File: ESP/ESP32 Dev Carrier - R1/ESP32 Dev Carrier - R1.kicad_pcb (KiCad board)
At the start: 4 copper layers, 75 x 75 mm, 57 parts, among them J1 Conn_01x02, J2 USB_B_Micro, J3 Conn_02x20_Top_Bottom, J4 Conn_01x05, J5 Conn_01x05, J6 Conn_01x05, Q1 MMS9013, Q2 MMS9013, SW1 SW_Push, U1 ESP32-WROVER-B_(16MB)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

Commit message: Blurgh. Almost ready to order.
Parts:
- added D10: BAT54S, Package_TO_SOT_SMD:SOT-23, F.Cu at (39.7, 44.1)
- added D11: BAT54S, Package_TO_SOT_SMD:SOT-23, F.Cu at (39.7, 34.0)
- added D13: BAT54S, Package_TO_SOT_SMD:SOT-23, F.Cu at (43.9, 36.5)
- added D14: BAT54S, Package_TO_SOT_SMD:SOT-23, F.Cu at (43.9, 41.6)
- added D15: BAT54S, Package_TO_SOT_SMD:SOT-23, F.Cu at (39.7, 39.0)
- added D16: BAT54S, Package_TO_SOT_SMD:SOT-23, F.Cu at (44.2, 11.8)
- added D17: BAT54S, Package_TO_SOT_SMD:SOT-23, F.Cu at (44.2, 15.6)
- added D5: BAT54S, Package_TO_SOT_SMD:SOT-23, F.Cu at (43.9, 51.7)
- added D6: BAT54S, Package_TO_SOT_SMD:SOT-23, F.Cu at (39.7, 49.2)
- added D9: BAT54S, Package_TO_SOT_SMD:SOT-23, F.Cu at (43.9, 46.7)
- added J10: Conn_01x09, Connector_JST:JST_XH_B9B-XH-A_1x09_P2.50mm_Vertical, F.Cu at (71.2, 34.2)
- added J11: Conn_01x04, Connector_JST:JST_XH_B4B-XH-A_1x04_P2.50mm_Vertical, F.Cu at (50.1, 20.1)
- added J12: Conn_01x04, Connector_JST:JST_XH_B4B-XH-A_1x04_P2.50mm_Vertical, F.Cu at (57.1, 20.0)
- added J13: Conn_01x04, Connector_JST:JST_XH_B4B-XH-A_1x04_P2.50mm_Vertical, F.Cu at (71.1, 20.1)
- added J14: Conn_01x04, Connector_JST:JST_XH_B4B-XH-A_1x04_P2.50mm_Vertical, F.Cu at (64.1, 20.1)
- added J7: Conn_01x09, Connector_JST:JST_XH_B9B-XH-A_1x09_P2.50mm_Vertical, F.Cu at (50.2, 34.2)
- added J8: Conn_01x09, Connector_JST:JST_XH_B9B-XH-A_1x09_P2.50mm_Vertical, F.Cu at (57.2, 34.2)
- added J9: Conn_01x09, Connector_JST:JST_XH_B9B-XH-A_1x09_P2.50mm_Vertical, F.Cu at (64.2, 34.2)
- added R18: 4.7K, Resistor_SMD:R_0603_1608Metric, F.Cu at (68.6, 60.0)
- added R19: 4.7K, Resistor_SMD:R_0603_1608Metric, F.Cu at (66.7, 60.0)
- added R20: 4.7K, Resistor_SMD:R_0603_1608Metric, F.Cu at (60.4, 60.0)
- added R21: 4.7K, Resistor_SMD:R_0603_1608Metric, F.Cu at (62.3, 60.0)
- added R22: 4.7K, Resistor_SMD:R_0603_1608Metric, F.Cu at (69.9, 14.9)
- added R23: 4.7K, Resistor_SMD:R_0603_1608Metric, F.Cu at (44.5, 29.5)
- D1: footprint Diode_SMD:D_SMA -> Diode_SMD:D_SMC
- J4, J5, J6: footprint Connector_JST:JST_XH_B5B-XH-AM_1x05_P2.50mm_Vertical -> Connector_JST:JST_XH_B5B-XH-A_1x05_P2.50mm_Vertical
- moved D8 62.7 mm to (63.5, 70.0)
- moved D12 62.4 mm to (61.6, 70.0)
- moved R27 62.4 mm to (63.5, 66.3)
- moved R10 62.1 mm to (61.6, 66.3)
- moved D3 47.8 mm to (57.8, 70.2)
- moved D4 47.4 mm to (55.9, 70.2)
- moved R13 42.7 mm to (57.8, 66.3)
- moved R16 42.3 mm to (55.9, 66.3)
- moved D7 36.7 mm to (59.7, 70.0)
- moved R26 36.7 mm to (59.7, 66.3)
- moved R14 25.7 mm to (69.9, 8.56), turned to 0 degrees
- moved R15 25.2 mm to (69.9, 11.1), turned to 0 degrees
- moved R6 25.1 mm to (43.9, 22.2), turned to -90 degrees
- moved R5 14.8 mm to (42.2, 22.2)
- moved J4 10.1 mm to (64.7, 3.64), turned to -90 degrees
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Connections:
- net Net-(J3-Pad27) renamed /IO4
- net Net-(J3-Pad29) renamed /IO2
- D3 pad 2: Net-(D3-Pad2) -> +3V3
- D4 pad 2: Net-(D4-Pad2) -> +3V3
- J3 pad 11: Net-(J3-Pad11) -> Net-(D10-Pad3)
- J4 pad 3: Net-(D2-Pad2) -> Net-(D2-Pad1)
- J4 pad 4: Net-(D2-Pad1) -> Net-(D2-Pad2)
- J5 pad 3: Net-(D2-Pad2) -> Net-(D2-Pad1)
- J5 pad 4: Net-(D2-Pad1) -> Net-(D2-Pad2)
- J6 pad 3: Net-(D2-Pad2) -> Net-(D2-Pad1)
- J6 pad 4: Net-(D2-Pad1) -> Net-(D2-Pad2)
- R13 pad 1: Net-(D3-Pad2) -> Net-(R13-Pad1)
- R13 pad 2: +3V3 -> Net-(D3-Pad1)
- R16 pad 1: Net-(D4-Pad2) -> Net-(R16-Pad1)
- R16 pad 2: +3V3 -> Net-(D4-Pad1)
- R27 pad 2: Net-(J3-Pad11) -> Net-(J3-Pad15)
- U1 pad 8: Net-(J3-Pad11) -> Net-(D10-Pad3)
- U4 pad 18: Net-(D4-Pad1) -> Net-(R16-Pad1)
- U4 pad 19: Net-(D3-Pad1) -> Net-(R13-Pad1)
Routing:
- net +5V: track 72.8 -> 223.0 mm, vias 5 -> 4
- net Net-(D10-Pad3): track 0.00 -> 100.6 mm, vias 0 -> 1
- net Net-(D11-Pad3): track 49.1 -> 140.5 mm, vias 1 -> 2
- net Net-(D13-Pad3): track 44.9 -> 128.5 mm, vias 1 -> 2
- net Net-(D15-Pad3): track 27.4 -> 107.8 mm, vias 1 -> 2
- net Net-(D14-Pad3): track 24.3 -> 101.7 mm, vias 1 -> 2
- net Net-(D5-Pad3): track 24.3 -> 100.5 mm
- net Net-(D6-Pad3): track 27.4 -> 103.2 mm
- net Net-(J3-Pad15): track 27.6 -> 101.9 mm
- net Net-(D9-Pad3): track 24.3 -> 98.4 mm
- net Net-(J3-Pad18): track 30.2 -> 91.9 mm
- net Net-(R13-Pad1): track 0.00 -> 56.8 mm
- net Net-(R16-Pad1): track 0.00 -> 55.1 mm
- net Net-(D17-Pad3): track 52.3 -> 105.4 mm
- net Net-(D16-Pad3): track 49.3 -> 98.1 mm
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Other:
- outline, holes or cut-outs redrawn
- board text added: "ESP32 DevCarrier"
- board text removed: "ESP32 DevBoard"

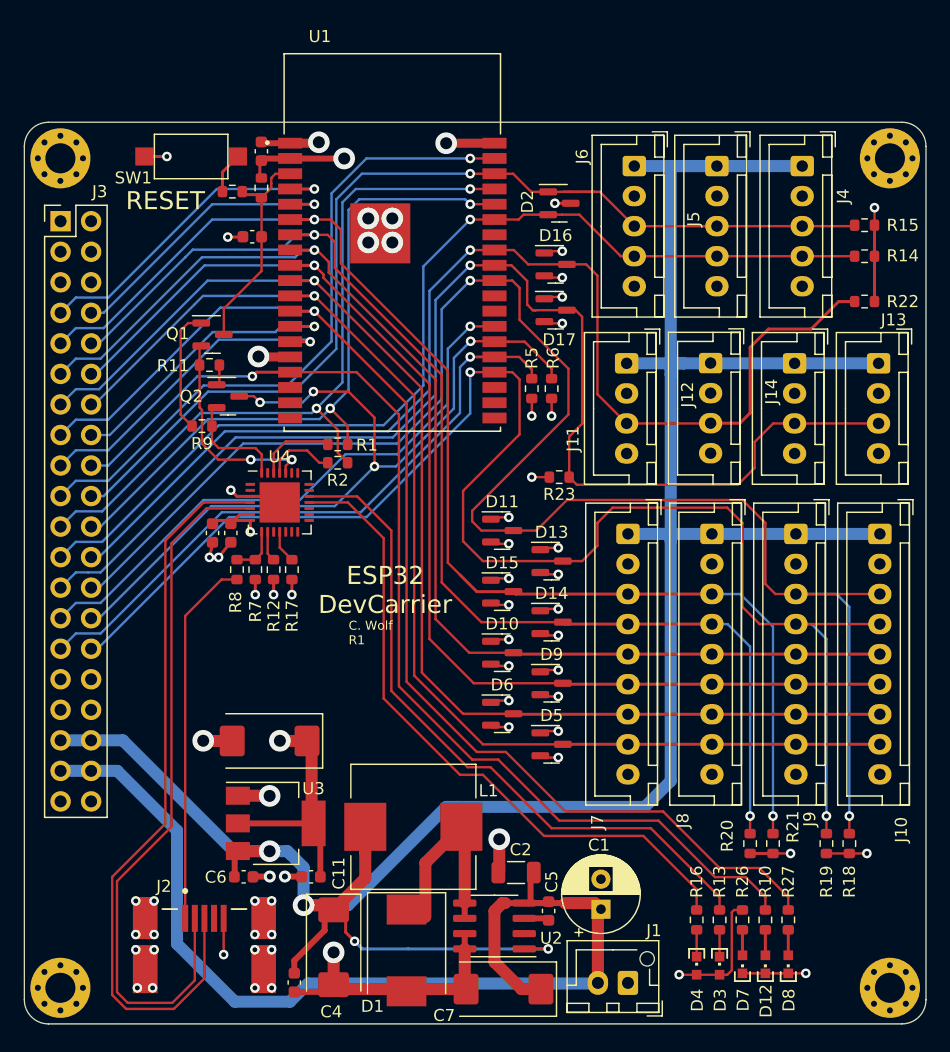
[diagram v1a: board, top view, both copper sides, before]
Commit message: Reworking things to use the new controller PCB.
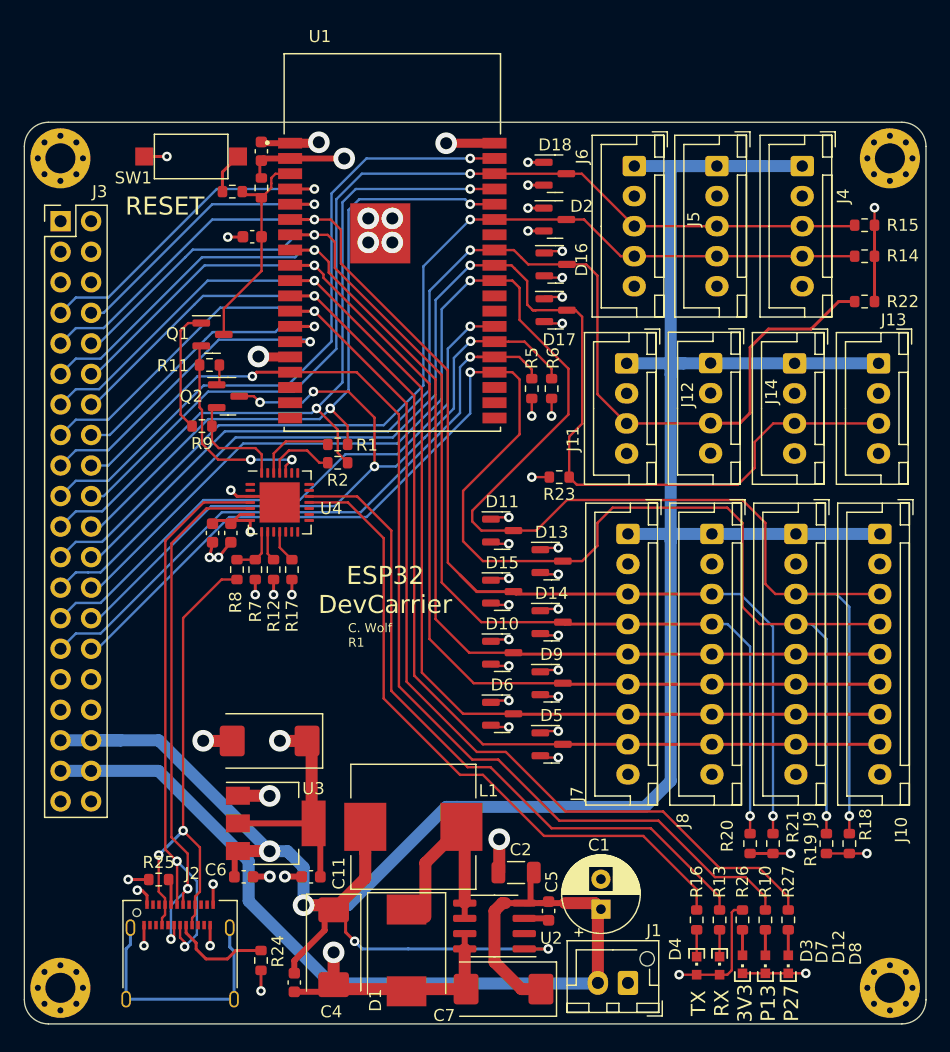
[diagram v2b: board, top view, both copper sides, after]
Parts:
- added D18: BAT54S, Package_TO_SOT_SMD:SOT-23, F.Cu at (44.1, 4.28)
- added R24: 5.1K, Resistor_SMD:R_0603_1608Metric, F.Cu at (19.7, 69.7)
- added R25: 5.1K, Resistor_SMD:R_0603_1608Metric, F.Cu at (11.2, 63.0)
- D2: value BAT54C -> BAT54S
- J2: value USB_B_Micro -> USB_C_Receptacle_USB2.0; footprint custom:Molex--0-0-0 -> Connector_USB:USB_C_Receptacle_Amphenol_12401610E4-2A
- moved J2 2.03 mm to (13.0, 70.1), turned to 0 degrees
- moved D2 1.40 mm to (44.1, 8.09)
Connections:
- net Net-(D10-Pad3) renamed /IO32
- net Net-(D11-Pad3) renamed /IO5
- net Net-(D13-Pad3) renamed /IO15
- net Net-(D14-Pad3) renamed /IO35
- net Net-(D15-Pad3) renamed /IO34
- net Net-(D16-Pad3) renamed /IO19
- net Net-(D17-Pad3) renamed /IO18
- net Net-(D5-Pad3) renamed /IO26
- net Net-(D6-Pad3) renamed /IO25
- net Net-(D9-Pad3) renamed /IO33
- net Net-(J3-Pad15) renamed /IO27
- net Net-(J3-Pad16) renamed /IO14
- net Net-(J3-Pad17) renamed /IO12
- net Net-(J3-Pad18) renamed /IO13
- net Net-(J3-Pad19) renamed /IO23
- net Net-(J3-Pad7) renamed /IO36
- net Net-(J3-Pad8) renamed /IO39
- net Net-(R13-Pad1) renamed /USB Interface/TXT
- net Net-(R16-Pad1) renamed /USB Interface/RXT
- D2 pad 1: Net-(D2-Pad1) -> GND
- D2 pad 2: Net-(D2-Pad2) -> +3V3
- D2 pad 3: +3V3 -> /IO21
- J3 pad 20: Net-(D2-Pad1) -> /IO22
- J3 pad 23: Net-(D2-Pad2) -> /IO21
- J4 pad 3: Net-(D2-Pad1) -> /IO22
- J4 pad 4: Net-(D2-Pad2) -> /IO21
- J5 pad 3: Net-(D2-Pad1) -> /IO22
- J5 pad 4: Net-(D2-Pad2) -> /IO21
- J6 pad 3: Net-(D2-Pad1) -> /IO22
- J6 pad 4: Net-(D2-Pad2) -> /IO21
- R14 pad 1: Net-(D2-Pad1) -> /IO22
- R15 pad 1: Net-(D2-Pad2) -> /IO21
- R8 pad 2: Net-(J2-Pad1) -> Net-(J2-PadA4)
- U1 pad 33: Net-(D2-Pad2) -> /IO21
- U1 pad 36: Net-(D2-Pad1) -> /IO22
- U4 pad 4: Net-(J2-Pad3) -> Net-(J2-PadA6)
- U4 pad 5: Net-(J2-Pad2) -> Net-(J2-PadA7)
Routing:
- net Net-(D2-Pad1): track 86.4 -> 0.00 mm, vias 1 -> 0
- net Net-(D2-Pad2): track 85.1 -> 0.00 mm, vias 1 -> 0
- net /IO21: track 0.00 -> 84.8 mm, vias 0 -> 1
- net /IO22: track 0.00 -> 83.8 mm, vias 0 -> 1
- net Net-(J2-Pad3): track 62.2 -> 0.00 mm
- net Net-(J2-Pad2): track 59.7 -> 0.00 mm
- net Net-(J2-PadA6): track 0.00 -> 49.2 mm, vias 0 -> 2
- net Net-(J2-PadA7): track 0.00 -> 44.6 mm, vias 0 -> 2
- net Net-(J2-PadA4): track 0.00 -> 41.2 mm, vias 0 -> 2
- net Net-(J2-Pad1): track 30.7 -> 0.00 mm
- net unconnected-(J2-PadS1): track 0.00 -> 21.2 mm
- net GND: track 81.4 -> 91.3 mm, vias 33 -> 40
- net Net-(J2-PadB5): track 0.00 -> 8.36 mm
- net VCC: track 87.4 -> 82.6 mm
- net +5V: track 223.0 -> 225.5 mm
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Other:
- board text added: "GND 3V GND IO36 IO34 IO32 IO25 IO27 IO12 IO23 MISO IO21 IO18 IO4 IO2 GND 3V3 5V0 VIN GND"
- board text added: "GND 3V GND IO39 IO35 IO33 IO26 IO14 IO13 IO22 MOSI IO19 IO5 PROG IO15 GND 3V3 5V0 VIN GND"
- board text added: "TX RX 3V3 P13 P27"
